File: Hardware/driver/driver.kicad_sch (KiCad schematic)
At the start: 6 parts, among them U102 DS2482-100

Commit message: Driver current zero adjustment
- Added facility on the driver board to adjust the zero offset for the
  current drive op amps, to allow them to actually reach zero when a
  zero DAC code is input to them.

  This is done by means of a -5V supply (generated with switched
  capacitor regulator) and each output amplifier having a -2.5V
  reference, and an associated multi-turn trim pot to actually trim
  that; these are hooked up to 3V3 digital on the other end (this should
  probably be the DAC reference but we don't have ez access to that)
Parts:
- added C101: 4.7µF, Capacitor_SMD:C_0805_2012Metric_Pad1.18x1.45mm_HandSolder, symbol Device:C_Small
- added C103, C104: 10µF, Capacitor_Tantalum_SMD:CP_EIA-3216-18_Kemet-A_Pad1.58x1.35mm_HandSolder, symbol Device:C_Polarized_Small
- added C105: 100nF, Capacitor_SMD:C_0805_2012Metric_Pad1.18x1.45mm_HandSolder, symbol Device:C_Small
- added TP101: -5V, TestPoint:TestPoint_Keystone_5000-5004_Miniature, symbol Connector:TestPoint
- added U101: ICL7660, Package_SO:SOIC-8_3.9x4.9mm_P1.27mm, symbol Regulator_SwitchedCapacitor:ICL7660
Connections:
- net GND: now also C101.2, C104.1, C105.2, U101.3 (GND)
- new net: C103.1, U101.2 (CAP+)
- new net: C103.2, U101.4 (CAP-)
- new net +5V: C101.1, U101.8 (V+)
- new net -5V: C104.2, C105.1, TP101.1, U101.5 (VOUT)
- no-connect marks 1 -> 3
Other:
- title: (none) -> Dual Programmable Load Driver

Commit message: External trigger input
- Added a basic Schmitt-trigger based external trigger input. There's a
  basic pulse shaping circuit attached to it, before its fed into the
  buffer, and then off to the main board to use as an interrupt line to
  control the system mode.
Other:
- added sheet External Trigger (trigger.kicad_sch)
- sheet External Interface ports: added TRIGGER; removed none

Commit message: Start work on remote VSense; driver board tweaks
- Use the DAC reference as the positive end of the null adjustment
  trimmers, rather than the +3V3 supply; this should make the adjustment
  actually useful and persistent rather than relying on the relationship
  between the 3V3 rail and the DAC's internal reference.

- Moved the 1Wire controller slightly to allow relocating the zero
  offset trimmer for the first channel

- Start work on remote VSense

  This works by selecting between either voltage sensing at the source
  terminals, or an external sense input connected to another set of
  terminals. These are switched by a latching relay (as to provide
  satisfying clicky noises) and then go into an op amp working as a
  differential amplifier; it performs a 50:1 gain (obviating the need
  for resistor dividers, and providing greater accuracy) and that then
  goes into the measurement ADC as normal.

  We have to still figure out how to drive the relay (probably just an
  IO expander?) and place those components on the board.
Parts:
- renumbered C103 to C102, C104 to C103, C105 to C104, C102 to C105

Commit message: Finished remote VSense support
- Laid out the VSense amp and analog-to-digital converter, as well as
  added an I2C IO expander to handle driving the latching relay to
  switch between internal and external sense.

  Also moved the input connector and some of the analog parts around to
  accomodate this all.

- Status indicator (with an extra GPIO on the IO expander) in the form
  of a single LED
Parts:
- added C106: 100nF, Capacitor_SMD:C_0805_2012Metric_Pad1.18x1.45mm_HandSolder, symbol Device:C_Small
- added D101: Red, LED_SMD:LED_0805_2012Metric_Pad1.15x1.40mm_HandSolder, symbol Device:LED_Small
- added R101: 1k, Resistor_SMD:R_0805_2012Metric_Pad1.20x1.40mm_HandSolder, symbol Device:R_Small
- added U103: PI4IOE5V9536, Package_SO:MSOP-8_3x3mm_P0.65mm, symbol programmable-load:PI4IOE5V9536
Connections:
- net +3V3: now also C106.1, R101.1, U103.8 (VCC)
- net GND: now also C106.2, U103.4 (GND)
- net I2C_SCL: now also U103.6 (SCL)
- net I2C_SDA: now also U103.7 (SDA)
- new net: D101.1 (K), U103.5 (P3)
- new net: D101.2 (A), R101.2
- new net SENSE_RST: U103.3 (P2)
- new net SENSE_SET: U103.2 (P1)
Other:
- sheet Input Stage ports: added RELAY_RESET, RELAY_SET; removed none
- note added: "-5V Regulator"
- note added: "I²C address: 0b1000001"
- moved on the sheet: C101, C102, C103, C104, TP101, U101

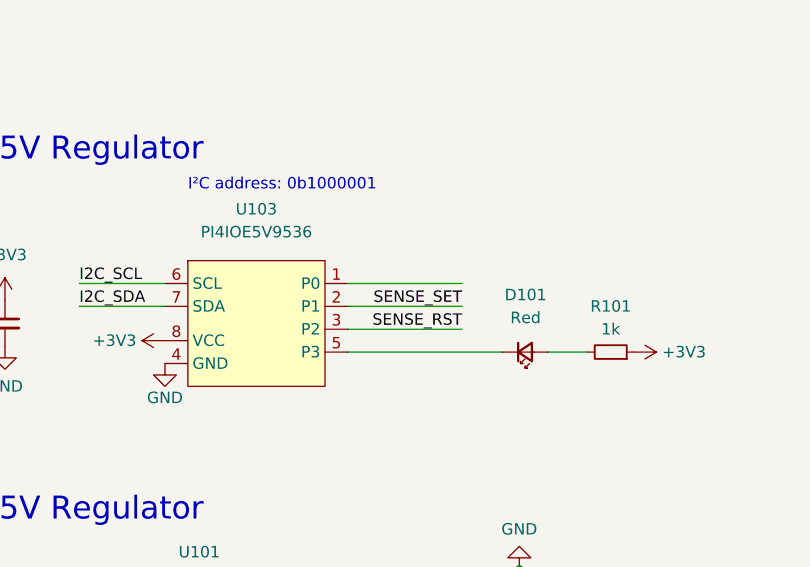
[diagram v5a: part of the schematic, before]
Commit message: Layout tweaks to driver
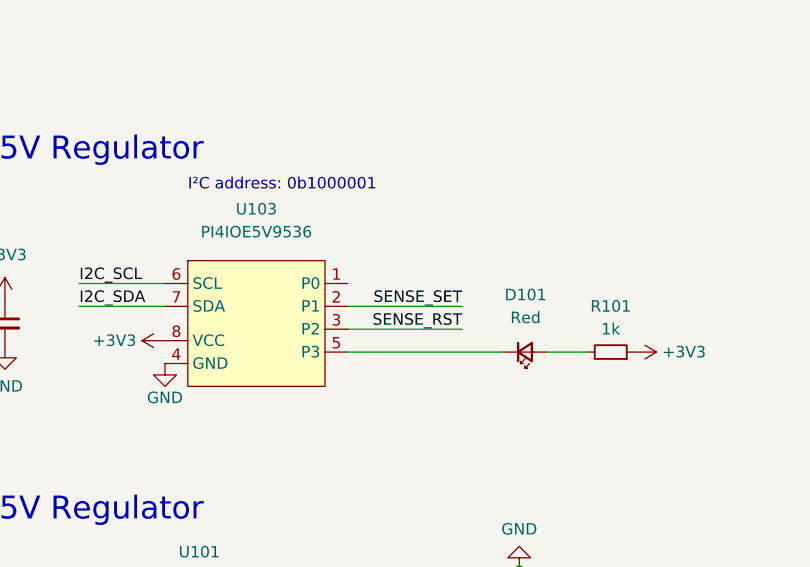
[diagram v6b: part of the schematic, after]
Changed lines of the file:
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@@
-    (stroke (width 0) (type default) (color 0 0 0 0))
-  )
-  (wire (pts (xy 62.23 123.19) (xy 74.93 123.19))
     (stroke (width 0) (type default) (color 0 0 0 0))
   )

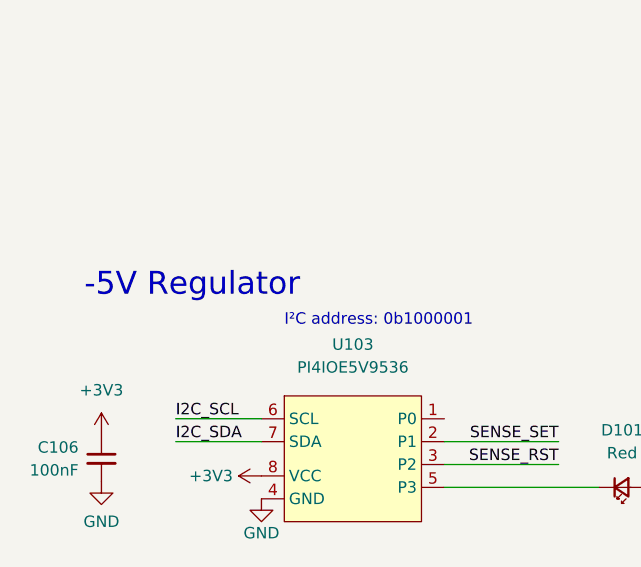
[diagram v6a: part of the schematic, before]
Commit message: Driver input protection; heatsink footprint tweaks
- Updated the footprint for the heatsink on the driver board to include
  a 3D model. Also fixed it… the distances were kind of out of whack and
  it would never have really fit

- Added a reverse polarity protection diode to the input; it gets its
  own cute little heatsink

- Minor movement to better accomodate a fan. A 20mm fan will likely
  interfere with the input connector (it might be worth switching to a
  different kind, or just soldering the connections altogether: spade
  terminals seem like a good choice for high current) and be very tight
  against the input diode's heatsink. We'll try with a 10mm fan and see
  if that's enough airflow.
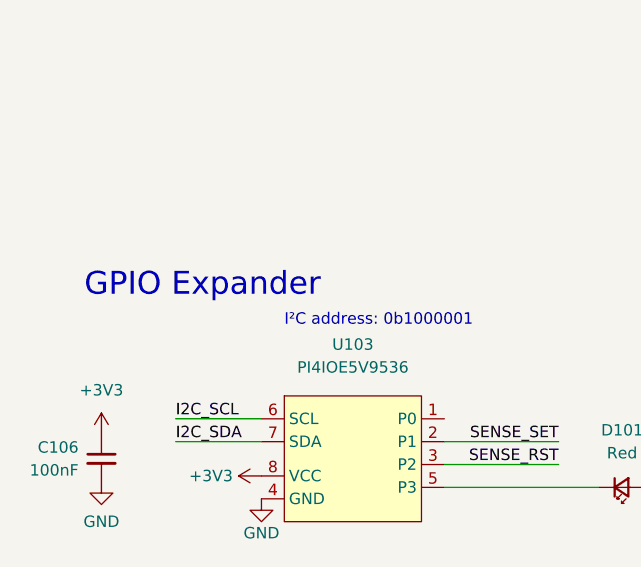
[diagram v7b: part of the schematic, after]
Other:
- note added: "GPIO Expander"
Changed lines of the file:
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@@
     (effects (font (size 1.27 1.27)) (justify left bottom))
   )
-  (text "-5V Regulator" (at 22.225 109.855 0)
+  (text "GPIO Expander" (at 22.225 109.855 0)
     (effects (font (size 2.54 2.54)) (justify left bottom))
   )
@@
       (reference "D203") (unit 1) (value "Red") (footprint "LED_SMD:LED_0805_2012Metric_Pad1.15x1.40mm_HandSolder")
     )
+    (path "/602636dc-d049-47b5-aa22-9e4cd7a5ce25/494dbac6-4432-4b87-8abb-b1023a21de1a"
+      (reference "D301") (unit 1) (value "DSA120C150QB") (footprint "Package_TO_SOT_THT:TO-247-3_Vertical")
+    )
     (path "/e84c78e9-1bd1-4873-b52a-cb877e8caf7e/03288cb1-6505-446e-b653-9038eaafb14d"
       (reference "D401") (unit 1) (value "SM6T22A") (footprint "Diode_SMD:D_SMB")
@@
       (reference "HS301") (unit 1) (value "2x C40-058-AE") (footprint "programmable-load:C40-058-AE-DUAL")
     )
+    (path "/602636dc-d049-47b5-aa22-9e4cd7a5ce25/672ae083-7804-4142-9a37-8284137926d7"
+      (reference "HS302") (unit 1) (value "WV-T247-101E") (footprint "programmable-load:Ohmite-WA-T247-101E-MFG")
+    )
     (path "/b8df6840-ecc7-4e2f-ad45-8c79faac2b74/f83f0a9a-85dc-4ae3-8b32-8863f8282cd1"
